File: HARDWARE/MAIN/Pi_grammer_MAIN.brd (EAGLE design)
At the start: 63.5 x 78.7 mm, 29 parts, among them J2 TARGET_copy, U1 AT42QT1010SOT23

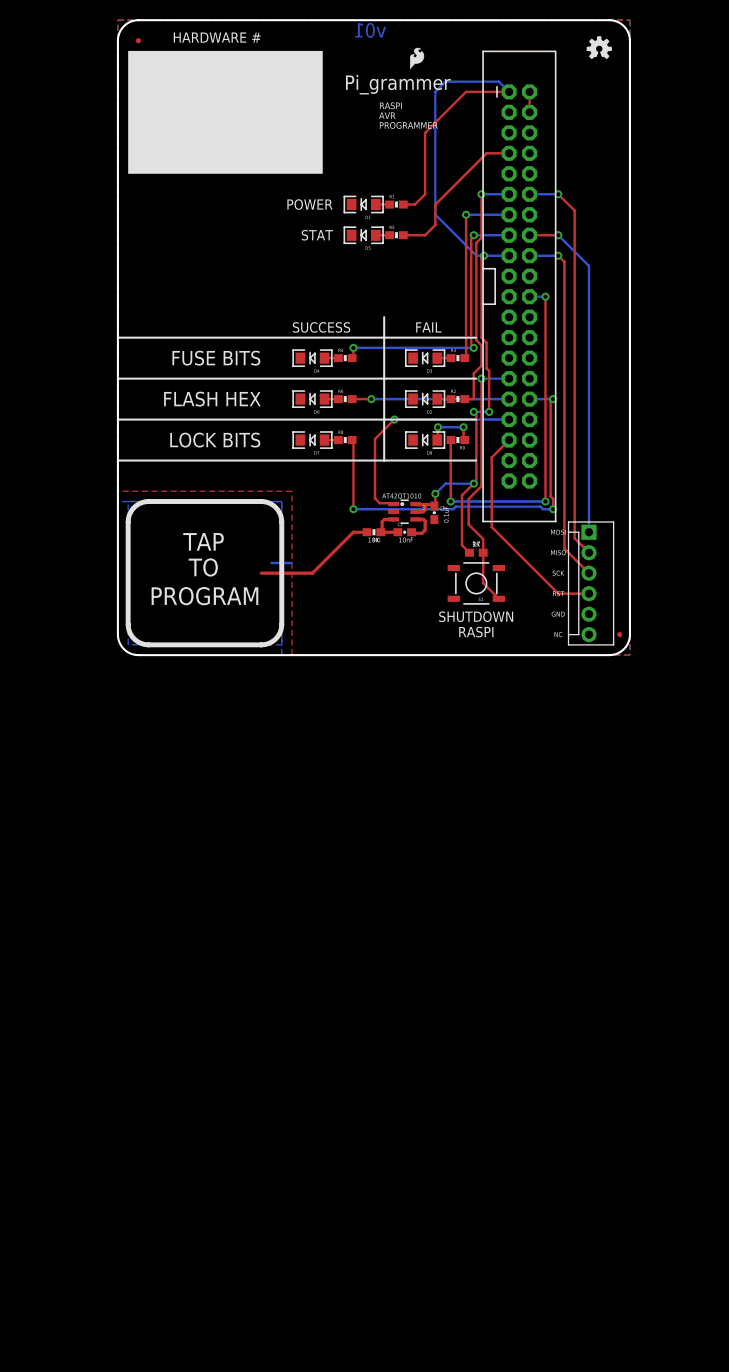
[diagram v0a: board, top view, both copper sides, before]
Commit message: SPI pins and llc
Just SCH work at this point.
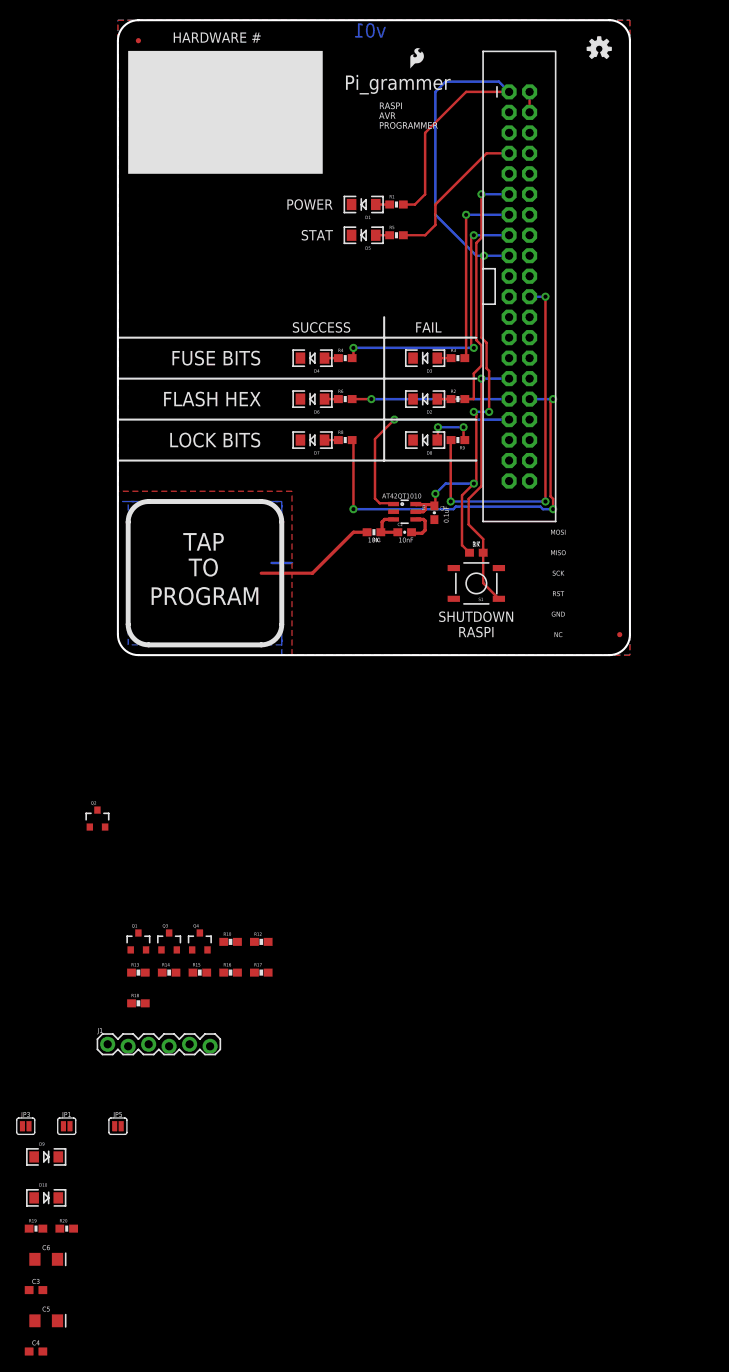
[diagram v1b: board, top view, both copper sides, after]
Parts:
- removed FRAME1: FRAME-LETTER, SparkFun-Aesthetics:CREATIVE_COMMONS
- removed J2: TARGET_copy, SparkFun-Connectors:MOLEX-1X6
- added C3, C4: 0.1uF, SparkFun-Capacitors:0603
- added C5, C6: 10uF, SparkFun-Capacitors:EIA3216
- added D10: RED, SparkFun-LED:LED-1206
- added D9: GREEN, SparkFun-LED:LED-1206
- added J1: TARGET_copy, SparkFun-Connectors:1X06-SIP_LOCK
- added JP1, JP3, JP5: (no value), SparkFun-Jumpers:SMT-JUMPER_2_NO_SILK
- added Q1, Q2, Q3, Q4: BSS138, SparkFun:SOT23-3
- added R10, R12, R13, R14, R15, R16, R17, R18: 10K, SparkFun:0603-RES
- added R19, R20: 1K, SparkFun-Resistors:0603-RES
- FD1, FD2: device SparkFun-Aesthetics:FIDUCIAL-MICRO -> SparkFun-Aesthetics:MICRO-FIDUCIAL
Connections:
- removed net GP26: JP2.37
- removed net SCLK: JP2.23
- new net N$12: JP1.1, JP3.1, JP5.1, R12.1, R14.1, R16.1, R18.1
- new net N$13: D9.A, R19.1
- new net N$14: D10.A, R20.1
- new net RST: JP2.37, Q2.2, R10.2
- new net SCK: JP2.23, Q1.2, R13.2
- new net SERIAL_UPLOAD_FAIL: R20.2
- new net SERIAL_UPLOAD_PASS: R19.2
- new net VCC_T: C4.1, C5.+, J1.6, JP5.2
- net 3.3V: now also C3.1, C6.+, JP1.2, Q1.1, Q2.1, Q3.1, Q4.1, R10.1, R13.1, R15.1, R17.1
- net 5V: now also JP3.2
- net GND: now also C3.2, C4.2, C5.-, C6.-, D10.C, D9.C, J1.5; no longer J2.5
- net MISO: now also Q3.2, R15.2
- net MISO_T: now also J1.2, Q3.3, R16.2; no longer J2.2, JP2.12
- net MOSI: now also Q4.2, R17.2
- net MOSI_T: now also J1.1, Q4.3, R18.2; no longer J2.1, JP2.16
- net RST_T: now also J1.4, Q2.3, R12.2; no longer J2.4, JP2.35
- net SCK_T: now also J1.3, Q1.3, R14.2; no longer J2.3, JP2.18
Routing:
- net MISO_T: track 49.6 -> 0.00 mm, vias 1 -> 0
- net SCK_T: track 44.5 -> 0.00 mm, vias 1 -> 0
- net MOSI_T: track 42.0 -> 0.00 mm, vias 1 -> 0
- net RST_T: track 27.2 -> 0.00 mm

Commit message: Initial part placement
still need to possibly swap out the capsense IC, so not gonna route
anything yet.

ALSO - the serial upload pins need to be connected to GPIO - need to
verify which pins can drive LEDs.
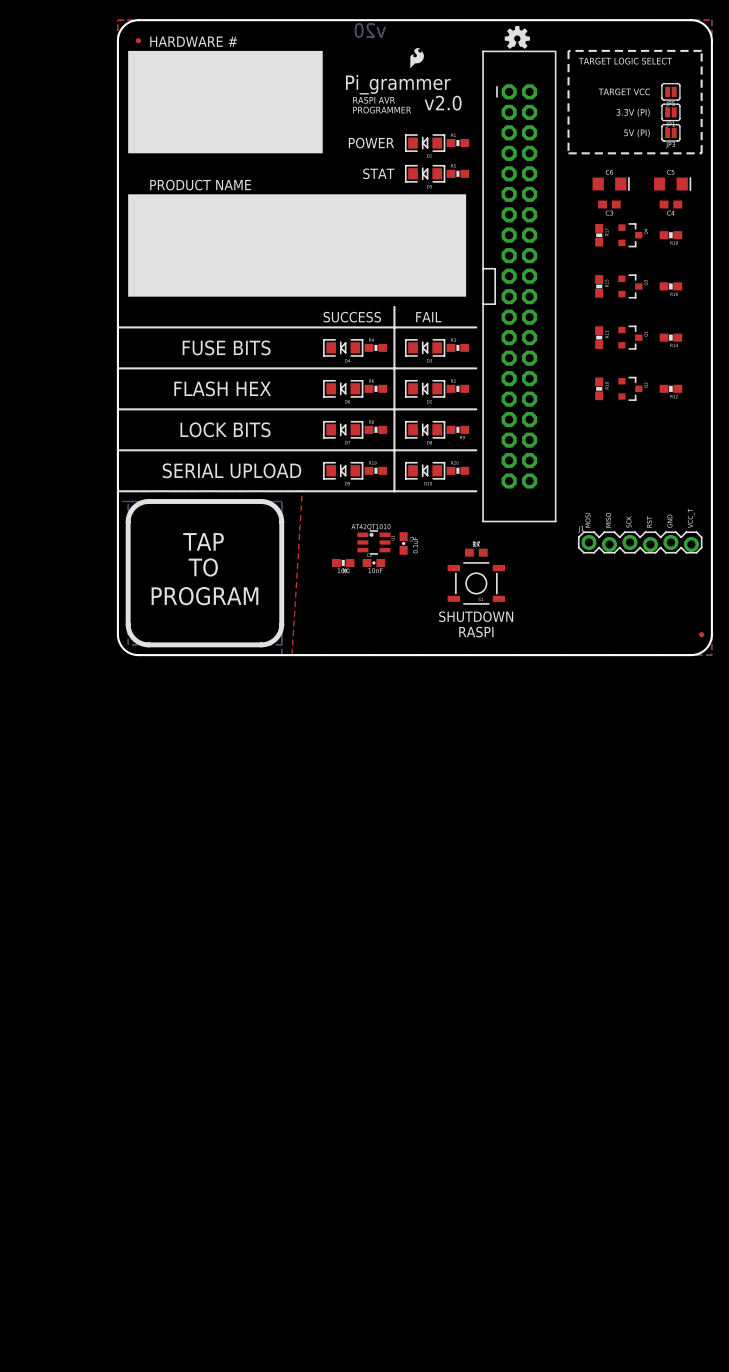
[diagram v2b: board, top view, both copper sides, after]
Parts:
- moved C4 162.6 mm to (68.6, 55.9), turned to 180 degrees
- moved C5 160.9 mm to (68.6, 58.4)
- moved C3 152.3 mm to (61.0, 55.9), turned to 180 degrees
- moved C6 150.5 mm to (61.0, 58.4)
- moved JP3 146.9 mm to (68.6, 64.8), turned to 180 degrees
- moved JP1 146.4 mm to (68.6, 67.3), turned to 180 degrees
- moved JP5 145.5 mm to (68.6, 69.8), turned to 180 degrees
- moved R18 115.9 mm to (68.6, 52.1), turned to 180 degrees
- moved R20 105.8 mm to (42.2, 22.9)
- moved R19 103.0 mm to (32.0, 22.9)
- moved Q4 102.6 mm to (63.5, 52.1), turned to 270 degrees
- moved D10 101.7 mm to (38.1, 22.9), turned to 180 degrees
- moved R16 101.1 mm to (68.6, 45.7), turned to 180 degrees
- moved R17 100.6 mm to (59.7, 52.1), turned to 270 degrees
- moved R14 100.4 mm to (68.6, 39.4), turned to 180 degrees
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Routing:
- net 3.3V: track 111.9 -> 0.00 mm, vias 5 -> 0
- net LOCK_BITS_PASS: track 50.6 -> 0.00 mm, vias 3 -> 0
- net LOCK_BITS_FAIL: track 46.8 -> 0.00 mm, vias 3 -> 0
- net FUSE_BITS_PASS: track 35.0 -> 0.00 mm, vias 3 -> 0
- net SHUTDOWN: track 32.9 -> 0.00 mm, vias 1 -> 0
- net FLASH_HEX_FAIL: track 30.9 -> 0.00 mm, vias 1 -> 0
- net CAPSENSE: track 27.8 -> 0.00 mm, vias 1 -> 0
- net FUSE_BITS_FAIL: track 23.3 -> 0.00 mm, vias 1 -> 0
- net FLASH_HEX_PASS: track 19.5 -> 0.00 mm, vias 1 -> 0
- net SCRIPT: track 18.8 -> 0.00 mm
- net PAD: track 15.2 -> 0.00 mm
- net N$8: track 6.59 -> 0.00 mm, vias 2 -> 0
- net N$11: track 5.00 -> 0.00 mm
- net N$10: track 4.29 -> 0.00 mm
- net GND: track 2.54 -> 0.00 mm
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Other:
- board size 63.5 x 78.7 mm -> 73.7 x 78.7 mm
- board text added: "3.3V (PI)"
- board text added: "5V (PI)"
- board text added: "PRODUCT NAME"
- board text added: "TARGET LOGIC SELECT"
- board text added: "TARGET VCC"
- board text added: "VCC_T"
- board text added: "v2.0"
- board text added: "v20"
- board text removed: "NC"
- board text removed: "Pete Lewis"
- board text removed: "v01"

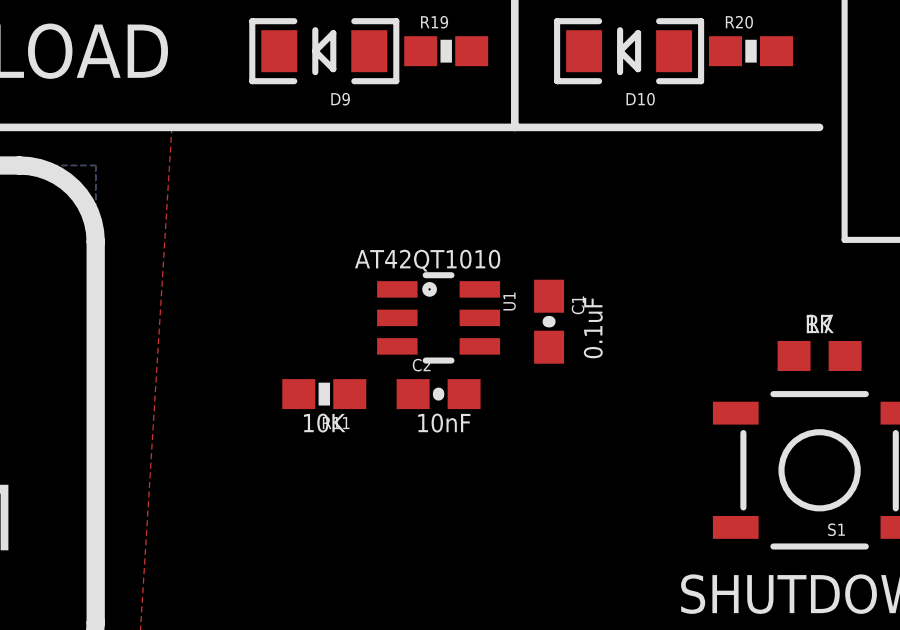
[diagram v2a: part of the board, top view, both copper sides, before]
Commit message: capsense IC replacement
trying out the UDFN package - dang that's tiny
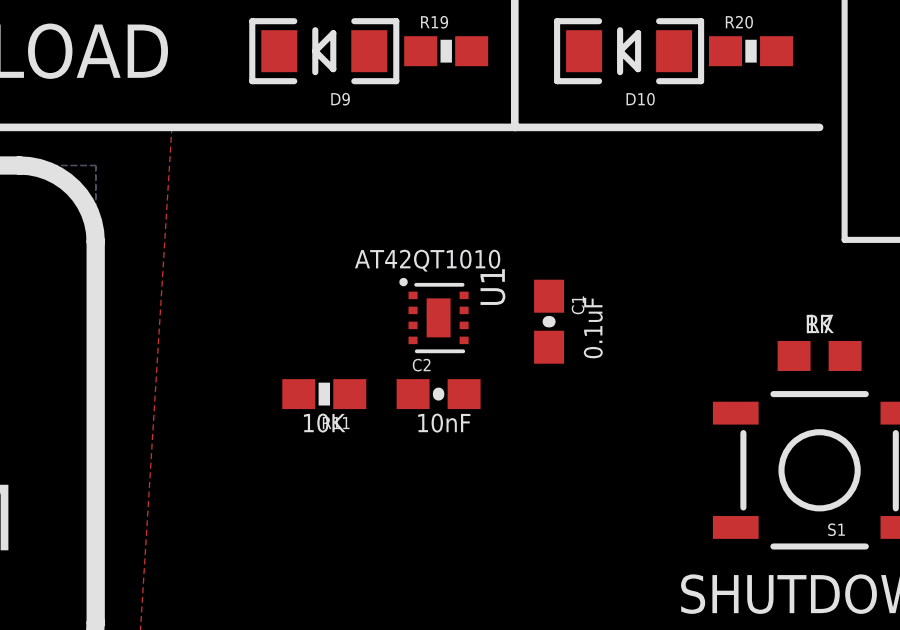
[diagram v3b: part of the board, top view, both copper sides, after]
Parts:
- U1: value AT42QT1010SOT23 -> AT42QT1010UDFN; device SparkFun-DigitalIC:SOT23-6 -> Testing:UDFN/USON_8_PAD
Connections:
- net 3.3V: now also U1.7; no longer U1.5
- net CAPSENSE: now also U1.5; no longer U1.1
- net GND: now also U1.4; no longer U1.2
- net N$10: now also U1.8; no longer U1.4
- net N$11: now also U1.1; no longer U1.3
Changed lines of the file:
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@@
 <layer number="47" name="Measures" color="7" fill="1" visible="no" active="yes"/>
 <layer number="48" name="Document" color="7" fill="1" visible="no" active="yes"/>
-<layer number="49" name="Reference" color="13" fill="1" visible="yes" active="yes"/>
+<layer number="49" name="Reference" color="13" fill="1" visible="no" active="yes"/>
 <layer number="50" name="dxf" color="7" fill="1" visible="no" active="yes"/>
 <layer number="51" name="tDocu" color="6" fill="1" visible="yes" active="yes"/>
@@
 <layer number="230" name="230bmp" color="7" fill="1" visible="no" active="yes"/>
 <layer number="231" name="231bmp" color="7" fill="1" visible="no" active="yes"/>
+<layer number="232" name="Eagle3D_PG2" color="7" fill="1" visible="yes" active="yes"/>
+<layer number="233" name="Eagle3D_PG3" color="7" fill="1" visible="yes" active="yes"/>
 <layer number="248" name="Housing" color="7" fill="1" visible="no" active="yes"/>
 <layer number="249" name="Edge" color="7" fill="1" visible="no" active="yes"/>
@@
 <element name="LOGO1" library="SparkFun-Aesthetics" package="SFE_LOGO_FLAME_.1" value="SFE_LOGO_FLAME.1_INCH" x="35.941" y="72.39"/>
 <element name="LOGO2" library="SparkFun-Aesthetics" package="OSHW-LOGO-S" value="OSHW-LOGOS" x="49.53" y="76.454"/>
-<element name="U1" library="SparkFun-DigitalIC" package="SOT23-6" value="AT42QT1010SOT23" x="31.75" y="13.97" rot="R270">
+<element name="U1" library="Testing" package="UDFN/USON_8_PAD" value="AT42QT1010UDFN" x="31.75" y="13.97" rot="R270">
 <attribute name="PROD_ID" value="IC-11778" x="31.75" y="13.97" size="1.778" layer="27" rot="R270" display="off"/>
 </element>
@@
 <contactref element="S1" pad="3"/>
 <contactref element="C1" pad="2"/>
-<contactref element="U1" pad="2"/>
+<contactref element="U1" pad="4"/>
 <polygon width="0.3048" layer="16" pour="hatch" isolate="0.3048">
 <vertex x="20.32" y="1.27"/>
@@
 <contactref element="R7" pad="1"/>
 <contactref element="U1" pad="6"/>
-<contactref element="U1" pad="5"/>
+<contactref element="U1" pad="7"/>
 <contactref element="C1" pad="1"/>
 <contactref element="Q2" pad="1"/>
@@
 <wire x1="43.6" y1="12.7" x2="59.69" y2="33.87" width="0" layer="19" extent="1-1"/>
 <wire x1="35.433" y1="14.693" x2="43.6" y2="12.7" width="0" layer="19" extent="1-1"/>
-<wire x1="33.1251" y1="14.92" x2="35.433" y2="14.693" width="0" layer="19" extent="1-1"/>
-<wire x1="33.1251" y1="13.97" x2="33.1251" y2="14.92" width="0" layer="19" extent="1-1"/>
+<wire x1="32.6016" y1="13.72" x2="35.433" y2="14.693" width="0" layer="19" extent="1-1"/>
+<wire x1="32.6016" y1="14.22" x2="32.6016" y2="13.72" width="0" layer="19" extent="1-1"/>
 </signal>
 <signal name="TXO">
@@
 </signal>
 <signal name="N$10">
-<contactref element="U1" pad="4"/>
+<contactref element="U1" pad="8"/>
 <contactref element="C2" pad="2"/>
-<wire x1="32.6" y1="11.43" x2="33.1251" y2="13.02" width="0" layer="19" extent="1-1"/>
+<wire x1="32.6" y1="11.43" x2="32.6016" y2="14.72" width="0" layer="19" extent="1-1"/>
 </signal>
 <signal name="N$11">
-<contactref element="U1" pad="3"/>
+<contactref element="U1" pad="1"/>
 <contactref element="R11" pad="1"/>
 <contactref element="C2" pad="1"/>
-<wire x1="30.9" y1="11.43" x2="30.3749" y2="13.02" width="0" layer="19" extent="1-1"/>
+<wire x1="30.9" y1="11.43" x2="30.8984" y2="14.72" width="0" layer="19" extent="1-1"/>
 <wire x1="28.79" y1="11.43" x2="30.9" y2="11.43" width="0" layer="19" extent="1-1"/>
 </signal>
@@
 <signal name="CAPSENSE">
 <contactref element="JP2" pad="33"/>
-<contactref element="U1" pad="1"/>
-<wire x1="30.3749" y1="14.92" x2="48.514" y2="29.21" width="0" layer="19" extent="1-1"/>
+<contactref element="U1" pad="5"/>
+<wire x1="32.6016" y1="13.22" x2="48.514" y2="29.21" width="0" layer="19" extent="1-1"/>
 </signal>
 <signal name="N$8">

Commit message: finished layout v20
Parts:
- moved C1 7.62 mm to (27.8, 14.1), turned to 180 degrees
- moved C5 1.02 mm to (67.6, 58.4)
- moved C4 0.52 mm to (68.1, 55.8)
- moved C3 0.51 mm to (61.5, 55.9)
- turned C2 to 180 degrees
- turned R9 to 0 degrees
- turned U1 to 90 degrees
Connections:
- removed net N$12: JP1.1, JP3.1, JP5.1, R12.1, R14.1, R16.1, R18.1
- new net N$9: C4.1, C5.+, JP1.1, JP3.1, JP5.1, R12.1, R14.1, R16.1, R18.1
- net SERIAL_UPLOAD_FAIL: now also JP2.18
- net SERIAL_UPLOAD_PASS: now also JP2.16
- net VCC_T: no longer C4.1, C5.+
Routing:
- net 3.3V: track 0.00 -> 154.4 mm, vias 0 -> 6
- net VCC_T: track 0.00 -> 65.0 mm
- net SERIAL_UPLOAD_FAIL: track 0.00 -> 52.3 mm, vias 0 -> 3
- net MOSI_T: track 0.00 -> 44.4 mm, vias 0 -> 1
- net SERIAL_UPLOAD_PASS: track 0.00 -> 41.6 mm, vias 0 -> 3
- net MISO_T: track 0.00 -> 37.2 mm, vias 0 -> 1
- net N$9: track 0.00 -> 37.2 mm
- net SHUTDOWN: track 0.00 -> 31.0 mm, vias 0 -> 1
- net FLASH_HEX_FAIL: track 0.00 -> 30.0 mm, vias 0 -> 1
- net LOCK_BITS_FAIL: track 0.00 -> 29.3 mm, vias 0 -> 1
- net SCK_T: track 0.00 -> 29.0 mm
- net CAPSENSE: track 0.00 -> 28.5 mm, vias 0 -> 1
- net FUSE_BITS_PASS: track 0.00 -> 25.1 mm
- net RST_T: track 0.00 -> 23.1 mm
- net 5V: track 0.00 -> 21.8 mm, vias 0 -> 1
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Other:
- board text removed: "GP20"
- board text removed: "GP21"

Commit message: updated SFE flame to proper polygon width dran package
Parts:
- LOGO1: value SFE_LOGO_FLAME.1_INCH -> SFE_LOGO_FLAME.2_INCH; device SparkFun-Aesthetics:SFE_LOGO_FLAME_.1 -> SparkFun-Aesthetics:SFE_LOGO_FLAME_.2
- moved LOGO1 1.65 mm to (34.3, 72.4)
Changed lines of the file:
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@@
 <layer number="47" name="Measures" color="7" fill="1" visible="no" active="yes"/>
 <layer number="48" name="Document" color="7" fill="1" visible="no" active="yes"/>
-<layer number="49" name="Reference" color="13" fill="1" visible="yes" active="yes"/>
+<layer number="49" name="Reference" color="13" fill="1" visible="no" active="yes"/>
 <layer number="50" name="dxf" color="7" fill="1" visible="no" active="yes"/>
 <layer number="51" name="tDocu" color="6" fill="1" visible="yes" active="yes"/>
@@
 <attribute name="VALUE" value="GREEN" x="27.94" y="27.94" size="1.778" layer="27" rot="R180" display="off"/>
 </element>
-<element name="LOGO1" library="SparkFun-Aesthetics" package="SFE_LOGO_FLAME_.1" value="SFE_LOGO_FLAME.1_INCH" x="35.941" y="72.39"/>
 <element name="LOGO2" library="SparkFun-Aesthetics" package="OSHW-LOGO-S" value="OSHW-LOGOS" x="49.53" y="76.454"/>
 <element name="U1" library="Testing" package="UDFN/USON_8_PAD" value="AT42QT1010UDFN" x="31.75" y="13.97" rot="R90">
@@
 <attribute name="PROD_ID" value="CAP-00811" x="67.564" y="54.61" size="1.778" layer="27" font="vector" ratio="15" display="off"/>
 </element>
+<element name="LOGO1" library="SparkFun-Aesthetics" package="SFE_LOGO_FLAME_.2" value="SFE_LOGO_FLAME.2_INCH" x="34.29" y="72.39"/>
 </elements>
 <signals>
